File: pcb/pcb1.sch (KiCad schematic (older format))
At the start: 18 parts, among them J1 Screw_Terminal_01x02, J2 Screw_Terminal_01x02, J3 USB_A, J4 CH340G - LEFT, J5 CH340G - RIGHT, K1 JQC-3F-_T73_-1Z-12VDC, K2 JQC-3F-_T73_-1Z-12VDC, Q1 BC547, Q2 BC547, U1 ATtiny85-20PU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

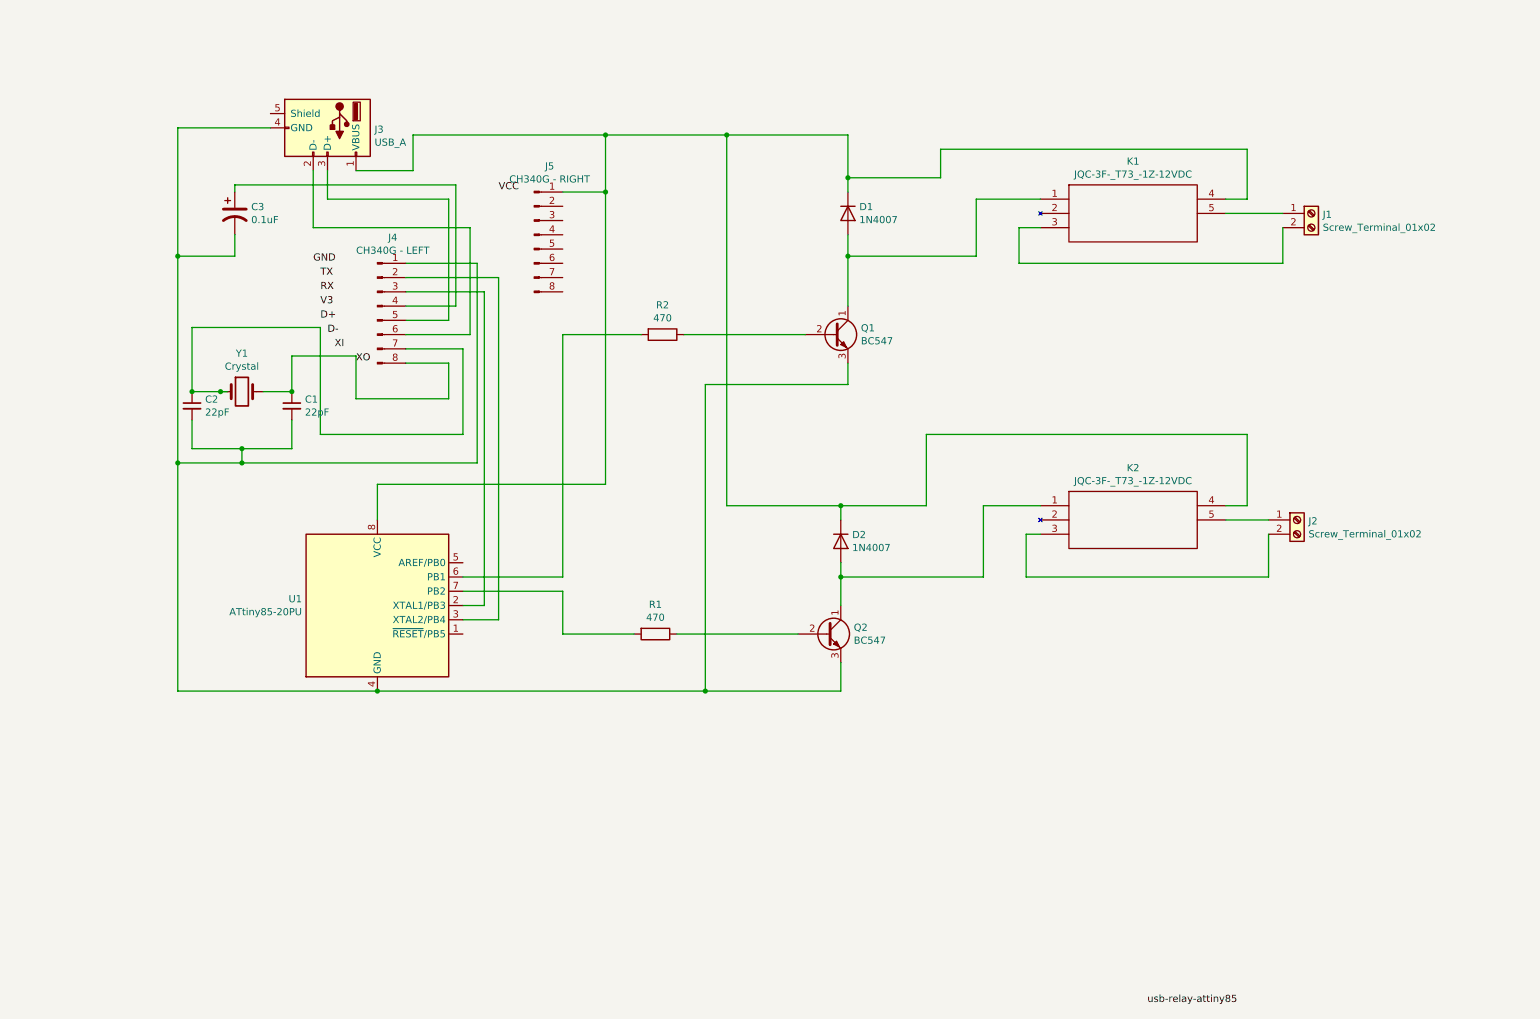
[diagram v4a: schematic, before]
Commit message: Finalized attiny85-multiplxed design
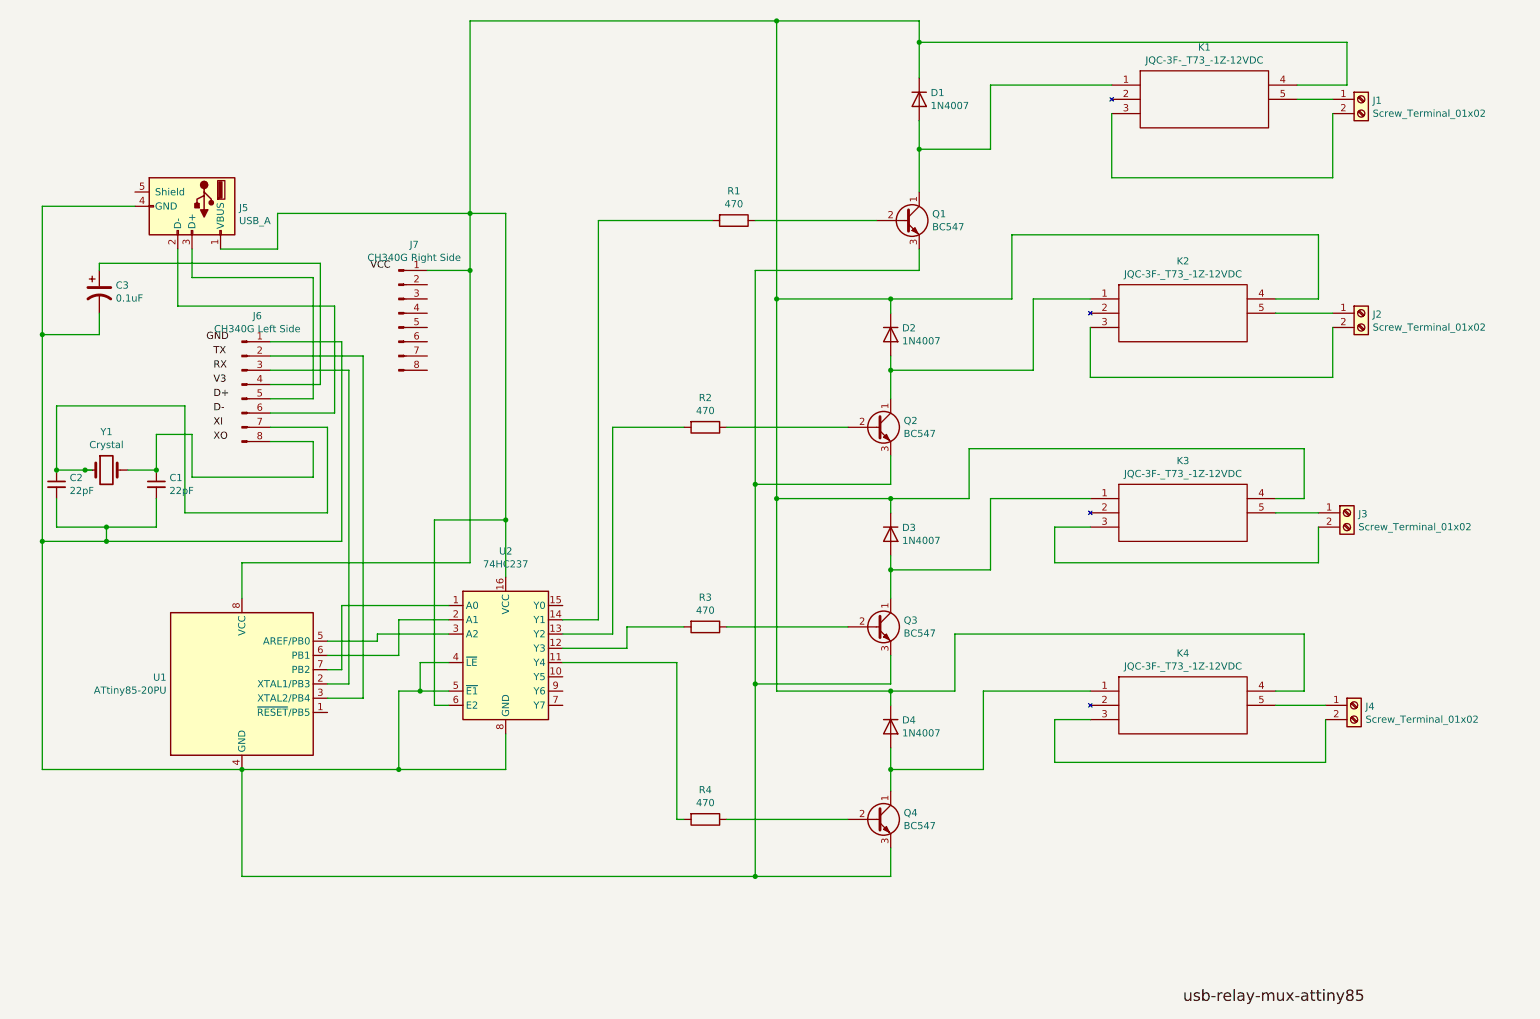
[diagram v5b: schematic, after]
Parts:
- added D3, D4: 1N4007, Diode_THT:D_DO-41_SOD81_P10.16mm_Horizontal, symbol Diode:1N4007
- added J3, J4: Screw_Terminal_01x02, TerminalBlock:TerminalBlock_Altech_AK300-2_P5.00mm, symbol Connector:Screw_Terminal_01x02
- added K3, K4: JQC-3F-_T73_-1Z-12VDC, JQC-3F-_T73_-1Z-12VDC:JQC3FT731Z12VDC, symbol JQC-3F-_T73_-1Z-12VDC:JQC-3F-_T73_-1Z-12VDC
- added Q3, Q4: BC547, Package_TO_SOT_THT:TO-92_Inline, symbol Transistor_BJT:BC547
- added R3, R4: 470, Resistor_THT:R_Axial_DIN0411_L9.9mm_D3.6mm_P12.70mm_Horizontal, symbol Device:R
- added U2: 74HC237, Package_DIP:DIP-16_W7.62mm, symbol 74xx:74HC237
- J6: renamed from J4; value CH340G - LEFT -> CH340G Left Side
- J7: renamed from J5; value CH340G - RIGHT -> CH340G Right Side
- renumbered J3 to J5, R2 to R1, R1 to R2
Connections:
- net XO: no longer C1.1, J6.8 (Pin_8), Y1.2
- net at C1.2, C2.2, C3.2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: now also Q3.3 (E), Q4.3 (E), U2.4 (~LE), U2.5 (~E1), U2.8 (GND)
- net at D1.1 (K), D2.1 (K), J5.1 (VBUS)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: now also D3.1 (K), D4.1 (K), K3.4, K4.4, U2.16 (VCC), U2.6 (E2)
- net at R2.2: now also U2.13 (Y2); no longer U1.7 (PB2)
- net at R1.2: now also U2.14 (Y1); no longer U1.6 (PB1)
- net at U1.5 (AREF/PB0): now also U2.3 (A2)
- new net: U1.6 (PB1), U2.2 (A1)
- new net: U1.7 (PB2), U2.1 (A0)
- new net: C1.1, J6.8 (Pin_8), Y1.2
- new net: R4.2, U2.11 (Y4)
- new net: R3.2, U2.12 (Y3)
- new net: D3.2 (A), K3.1, Q3.1 (C)
- new net: Q3.2 (B), R3.1
- new net: J3.2 (Pin_2), K3.3
- new net: J3.1 (Pin_1), K3.5
- new net: D4.2 (A), K4.1, Q4.1 (C)
- new net: Q4.2 (B), R4.1
- new net: J4.2 (Pin_2), K4.3
- new net: J4.1 (Pin_1), K4.5
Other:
- moved on the sheet: C1, C2, C3, D1, D2, J1, J2, J5, J6, J7, K1, K2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

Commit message: Finalized atmega328p-through hole design
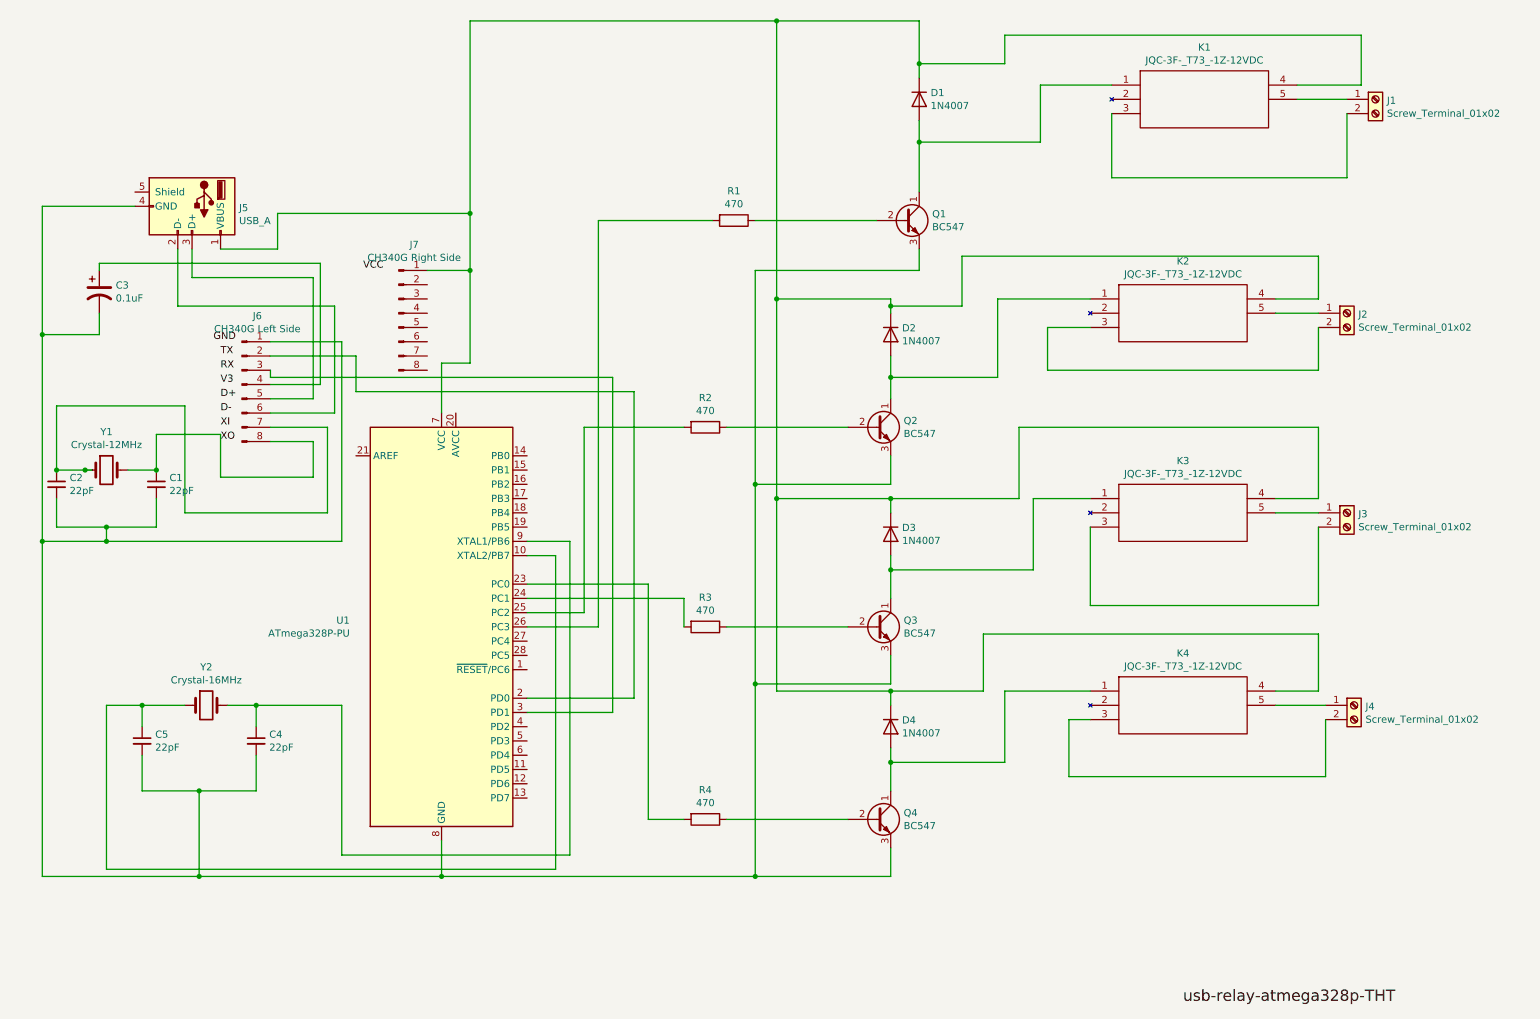
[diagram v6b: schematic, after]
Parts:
- removed U1: ATtiny85-20PU, Package_DIP:DIP-8_W7.62mm, symbol MCU_Microchip_ATtiny:ATtiny85-20PU
- removed U2: 74HC237, Package_DIP:DIP-16_W7.62mm, symbol 74xx:74HC237
- added C4, C5: 22pF, Capacitor_THT:C_Disc_D5.0mm_W2.5mm_P5.00mm, symbol Device:C_Small
- added U1: ATmega328P-PU, Package_DIP:DIP-28_W7.62mm, symbol MCU_Microchip_ATmega:ATmega328P-PU
- added Y2: Crystal-16MHz, Crystal:Crystal_HC49-4H_Vertical, symbol Device:Crystal
- Y1: value Crystal -> Crystal-12MHz
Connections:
- net XO: now also C1.1, J6.8 (Pin_8), Y1.2
- net at C1.2, C2.2, C3.2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: now also C4.2, C5.2, U1.22 (GND), U1.8 (GND)
- net at D1.1 (K), D2.1 (K), D3.1 (K)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: now also U1.7 (VCC)
- net at R2.2: now also U1.25 (PC2)
- net at R1.2: now also U1.26 (PC3)
- net at J6.3 (Pin_3): now also U1.3 (PD1)
- net at J6.2 (Pin_2): now also U1.2 (PD0)
- net at R4.2: now also U1.23 (PC0)
- net at R3.2: now also U1.24 (PC1)
- new net: C5.1, U1.10 (XTAL2/PB7), Y2.1
- new net: C4.1, U1.9 (XTAL1/PB6), Y2.2
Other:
- moved on the sheet: J1, J2

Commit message: Finalized atmega328p- SMD design
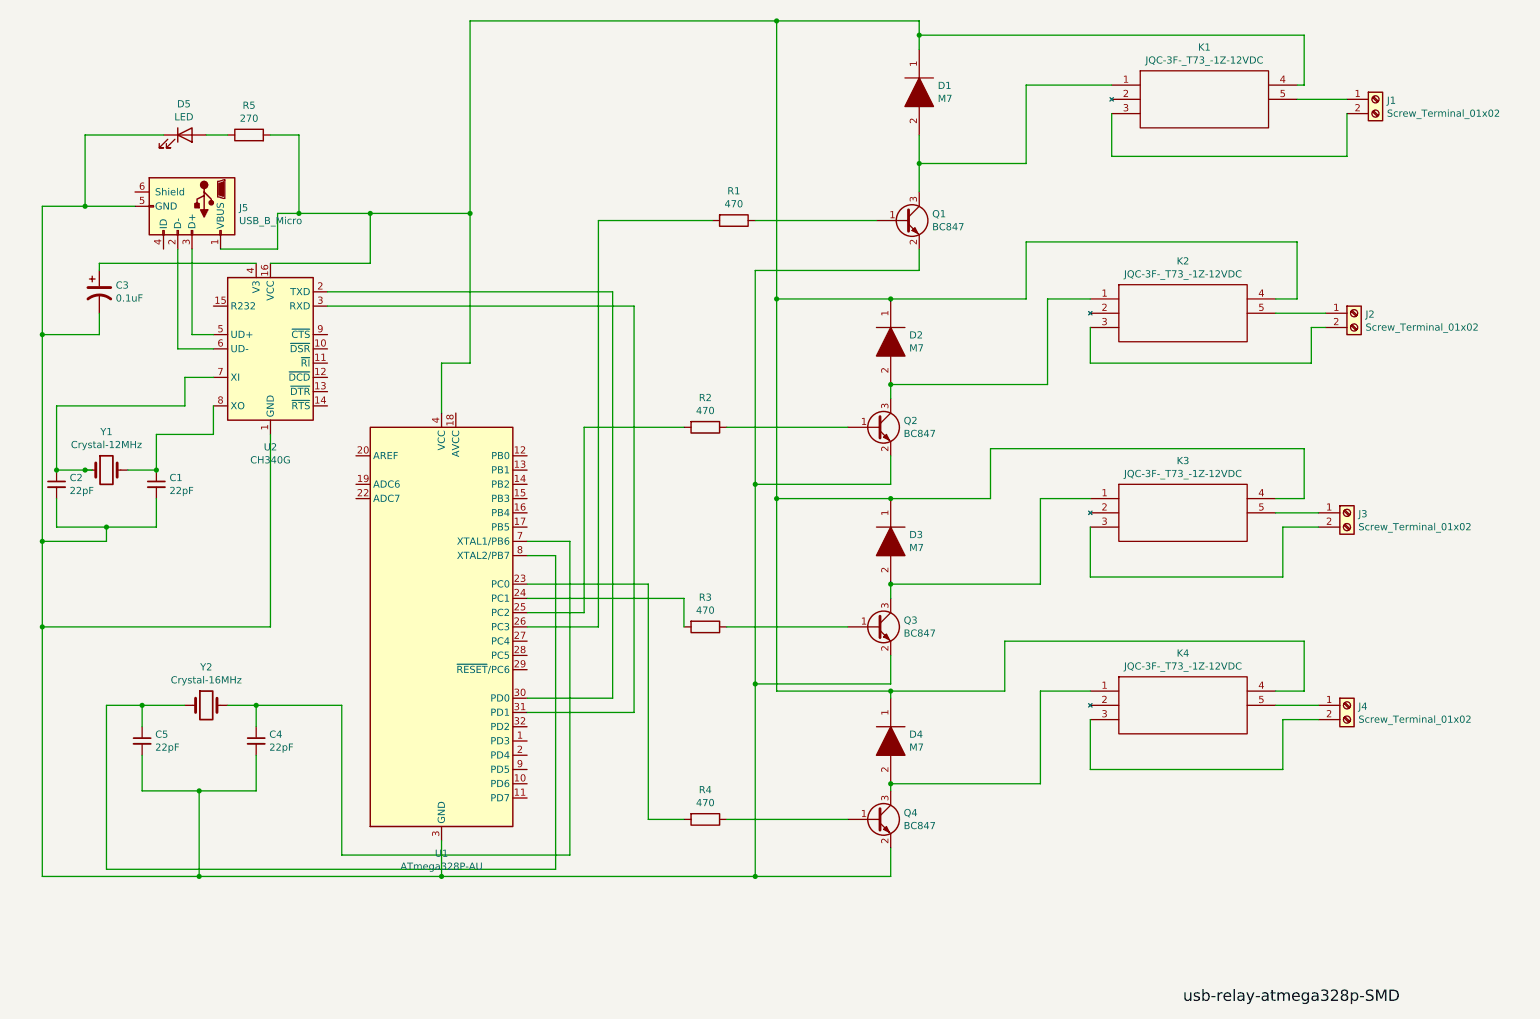
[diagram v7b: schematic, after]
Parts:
- removed D1, D2, D3, D4: 1N4007, Diode_THT:D_DO-41_SOD81_P10.16mm_Horizontal, symbol Diode:1N4007
- removed J5: USB_A, Connector_USB:USB_A_Molex_105057_Vertical, symbol Connector:USB_A
- removed J6: CH340G Left Side, Connector_PinHeader_2.54mm:PinHeader_1x08_P2.54mm_Horizontal, symbol Connector:Conn_01x08_Male
- removed J7: CH340G Right Side, Connector_PinHeader_2.54mm:PinHeader_1x08_P2.54mm_Horizontal, symbol Connector:Conn_01x08_Male
- removed Q1, Q2, Q3, Q4: BC547, Package_TO_SOT_THT:TO-92_Inline, symbol Transistor_BJT:BC547
- removed U1: ATmega328P-PU, Package_DIP:DIP-28_W7.62mm, symbol MCU_Microchip_ATmega:ATmega328P-PU
- added D1, D2, D3, D4: M7, M7:DIOM5626X245N, symbol M7:M7
- added D5: LED, LED_SMD:LED_0201_0603Metric, symbol Device:LED
- added J5: USB_B_Micro, Connector_USB:USB_Micro-B_Molex-105017-0001, symbol Connector:USB_B_Micro
- added Q1, Q2, Q3, Q4: BC847, Package_TO_SOT_SMD:SOT-23, symbol Transistor_BJT:BC847
- added R5: 270, Resistor_SMD:R_0201_0603Metric, symbol Device:R
- added U1: ATmega328P-AU, Package_QFP:TQFP-32_7x7mm_P0.8mm, symbol MCU_Microchip_ATmega:ATmega328P-AU
- added U2: CH340G, Package_SO:SOIC-16_3.9x9.9mm_P1.27mm, symbol Interface_USB:CH340G
- C1, C2, C4, C5: footprint Capacitor_THT:C_Disc_D5.0mm_W2.5mm_P5.00mm -> Capacitor_SMD:C_0201_0603Metric
- C3: footprint Capacitor_THT:CP_Radial_D5.0mm_P2.00mm -> Capacitor_SMD:CP_Elec_3x5.3
- R1, R2, R3, R4: footprint Resistor_THT:R_Axial_DIN0411_L9.9mm_D3.6mm_P12.70mm_Horizontal -> Resistor_SMD:R_0201_0603Metric
- Y1, Y2: footprint Crystal:Crystal_HC49-4H_Vertical -> Crystal:Crystal_SMD_HC49-SD
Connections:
- net at K1.1: now also D1.2, Q1.3 (C)
- net at R1.1: now also Q1.1 (B)
- net at C1.2, C2.2, C3.2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: now also D5.1 (K), J5.5 (GND), Q1.2 (E), Q2.2 (E), Q3.2 (E), Q4.2 (E), U1.21 (GND), U1.3 (GND), U1.5 (GND), U2.1 (GND)
- net at K2.1: now also D2.2, Q2.3 (C)
- net at R2.1: now also Q2.1 (B)
- net at K1.4, K2.4, K3.4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: now also D1.1, D2.1, D3.1, D4.1, J5.1 (VBUS), R5.2, U1.4 (VCC), U1.6 (VCC), U2.16 (VCC)
- net at R2.2: now also U1.25 (PC2)
- net at R1.2: now also U1.26 (PC3)
- net at C3.1: now also U2.4 (V3)
- net at C2.1, Y1.1: now also U2.7 (XI)
- net at K3.1: now also D3.2, Q3.3 (C)
- net at R3.1: now also Q3.1 (B)
- net at R3.2: now also U1.24 (PC1)
- net at C5.1, Y2.1: now also U1.8 (XTAL2/PB7)
- net at R4.2: now also U1.23 (PC0)
- net at C4.1, Y2.2: now also U1.7 (XTAL1/PB6)
- net at K4.1: now also D4.2, Q4.3 (C)
- net at R4.1: now also Q4.1 (B)
- net XO: no longer names the net of C1.1, Y1.2
- net XO: now also U2.8 (XO)
- new net: U1.30 (PD0), U2.2 (TXD)
- new net: U1.31 (PD1), U2.3 (RXD)
- new net: J5.3 (D+), U2.5 (UD+)
- new net: J5.2 (D-), U2.6 (UD-)
- new net: D5.2 (A), R5.1
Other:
- moved on the sheet: J2, J4
